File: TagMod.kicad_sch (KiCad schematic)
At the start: 9 parts, among them J101 Conn_ARM_JTAG_SWD_20, J103 Conn_ARM_JTAG_SWD_10

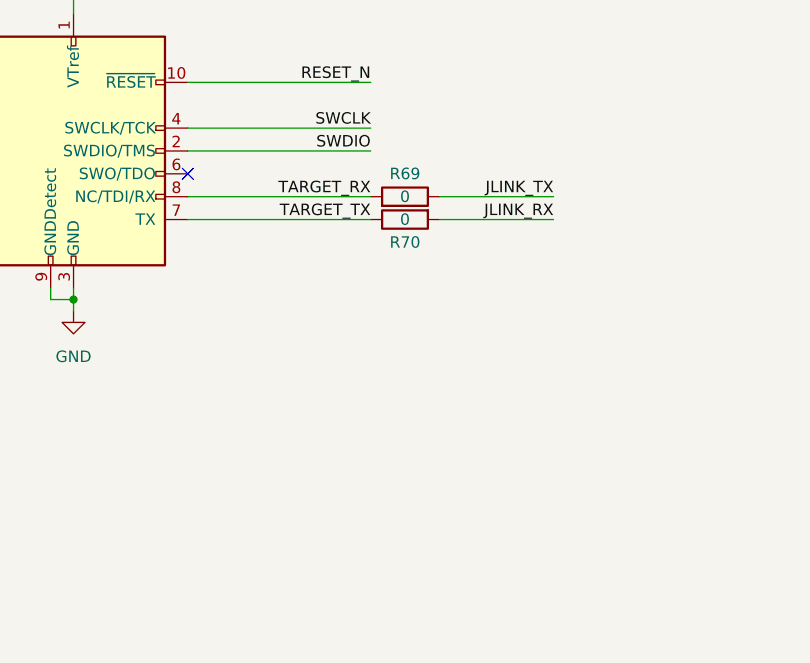
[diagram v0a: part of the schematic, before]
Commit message: rename project files to match repo and swap tx/rx
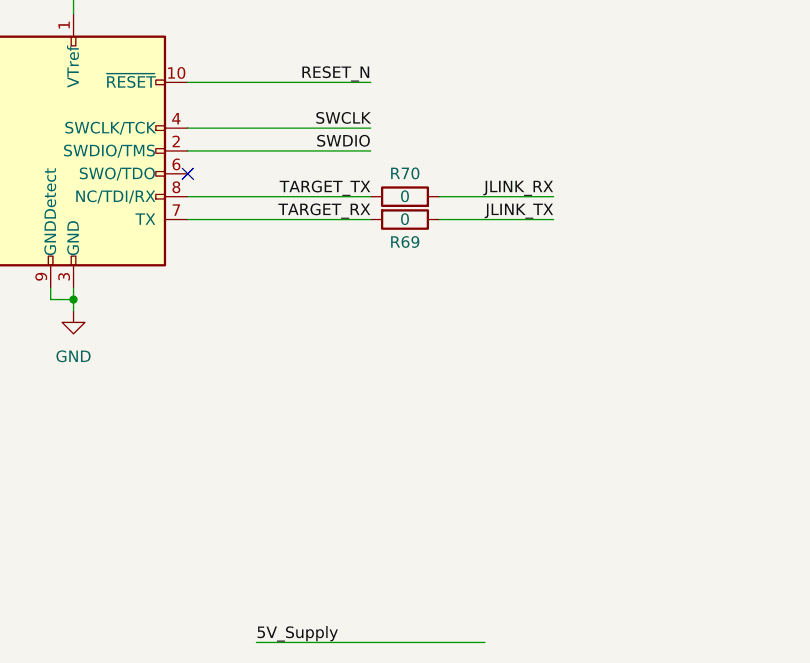
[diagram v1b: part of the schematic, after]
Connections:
- net TARGET_RX: now also J103.7 (TX); no longer J103.8 (NC/TDI/RX)
- net TARGET_TX: now also J103.8 (NC/TDI/RX); no longer J103.7 (TX)
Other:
- moved on the sheet: R69, R70

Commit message: rev b passes drc, ready for fab
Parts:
- added C1: CL21A106KAYNNNE, easyeda2kicad:C0805, symbol easyeda2kicad:CL21A106KAYNNNE
- added C2: CL10B224KA8NNNC, easyeda2kicad:C0603, symbol easyeda2kicad:CL10B224KA8NNNC
- added D1, D2: CUS10S30,H3F, easyeda2kicad:SOD-323_L1.8-W1.3-LS2.5-RD, symbol easyeda2kicad:CUS10S30,H3F
- added J1: Conn_01x03_Pin, Connector_PinHeader_2.54mm:PinHeader_1x03_P2.54mm_Vertical, symbol Connector:Conn_01x03_Pin
- added R2, R3, R4: 5K1, Resistor_SMD:R_0603_1608Metric, symbol Device:R_Small
- added R5: 2K7, Resistor_SMD:R_0603_1608Metric, symbol Device:R_Small
- added R6: 10K, Resistor_SMD:R_0603_1608Metric, symbol Device:R_Small
- added R7: 22K7, Resistor_SMD:R_0603_1608Metric, symbol Device:R_Small
- added R8: 6K1, Resistor_SMD:R_0603_1608Metric, symbol Device:R_Small
- added U1: AMS1117-ADJOFC, easyeda2kicad:SOT-89-3_L4.5-W2.5-P1.50-LS4.1-BR-1, symbol easyeda2kicad:AMS1117-ADJOFC
- added U2, U3: F.0603.00139/P2-0603R1TS2-06T-002, easyeda2kicad:LED0603-RD, symbol easyeda2kicad:F.0603.00139_P2-0603R1TS2-06T-002
- added U4: GT-USB-7010ASV, easyeda2kicad:USB-C-SMD_G-SWITCH_GT-USB-7010ASV, symbol easyeda2kicad:GT-USB-7010ASV
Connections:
- net 5V_Supply: now also D1.2 (A)
- net GND: now also C1.1, C2.1, R2.1, R3.1, R4.2, R5.2, R6.2, U4.A1B12 (GND), U4.B1A12 (GND)
- net VOUT: now reaches J103.6 (SWO/TDO)
- net VOUT: now also C1.2, R7.1, R8.1, U1.2 (Vout), U2.2 (A)
- new net: R4.1, U3.1 (K)
- new net: R5.1, U2.1 (K)
- new net: J1.1 (Pin_1), R8.2
- new net: J1.3 (Pin_3), R7.2
- new net: D1.1 (K), D2.1 (K), U1.3 (Vin), U3.2 (A)
- new net: R3.2, U4.A5 (CC1)
- new net: R2.2, U4.B5 (CC2)
- new net ADJ: C2.2, J1.2 (Pin_2), R6.1, U1.1 (ADJ)
- new net USB-VBUS: D2.2 (A), U4.A4B9 (VBUS), U4.B4A9 (VBUS)
- no-connect marks 1 -> 0
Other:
- note added: "20 pin JLink interface"
- moved on the sheet: J101, J103, R67, R68, R69, R70
